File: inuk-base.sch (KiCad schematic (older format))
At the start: 4 parts

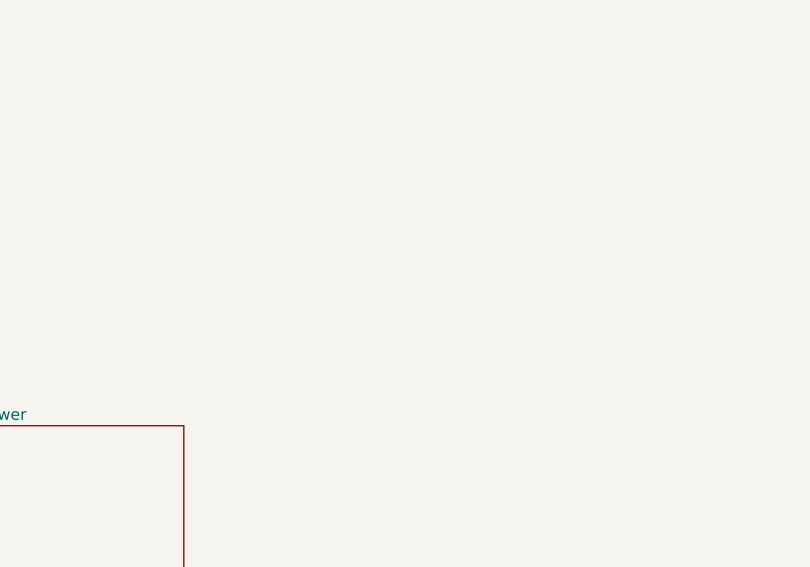
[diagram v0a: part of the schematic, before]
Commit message: created light control schematic
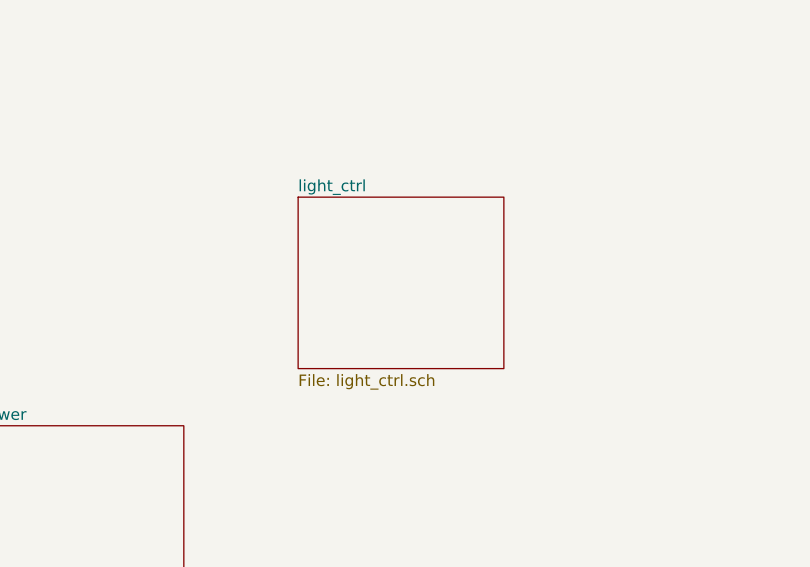
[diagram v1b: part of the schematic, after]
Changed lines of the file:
@@
 $Descr A4 11693 8268
 encoding utf-8
-Sheet 1 4
+Sheet 1 5
 Title ""
 Date ""
@@
 	1    0    0    -1
 $EndComp
+$Sheet
+S 6850 2350 900  750
+U 5E8399F7
+F0 "light_ctrl" 50
+F1 "light_ctrl.sch" 50
+$EndSheet
 $EndSCHEMATC

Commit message: layout
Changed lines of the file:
@@
 $EndDescr
 $Sheet
-S 2750 1750 1150 1400
+S 3750 2700 1150 1400
 U 5E59E010
 F0 "cpu" 50
 F1 "cpu.sch" 50
-F2 "uart_tx" O R 3900 1850 50
-F3 "uart_cts" I R 3900 2150 50
-F4 "uart_rts" O R 3900 2050 50
-F5 "uart_rx" I R 3900 1950 50
+F2 "uart_tx" O R 4900 2800 50
+F3 "uart_cts" I R 4900 3100 50
+F4 "uart_rts" O R 4900 3000 50
+F5 "uart_rx" I R 4900 2900 50
 $EndSheet
 $Sheet
-S 4400 1750 700  500
+S 5400 2700 700  500
 U 5E5A7255
 F0 "uart" 50
 F1 "uart.sch" 50
-F2 "uart_tx" I L 4400 1850 50
-F3 "uart_cts" O L 4400 2150 50
-F4 "uart_rts" I L 4400 2050 50
-F5 "uart_rx" O L 4400 1950 50
+F2 "uart_tx" I L 5400 2800 50
+F3 "uart_cts" O L 5400 3100 50
+F4 "uart_rts" I L 5400 3000 50
+F5 "uart_rx" O L 5400 2900 50
 $EndSheet
 $Sheet
-S 5450 3350 900  750
+S 5800 4300 900  750
 U 5E5BC499
 F0 "power" 50
@@
 $EndSheet
 Wire Wire Line
-	4400 1850 3900 1850
+	5400 2800 4900 2800
 Wire Wire Line
-	3900 1950 4400 1950
+	4900 2900 5400 2900
 Wire Wire Line
-	3900 2050 4400 2050
+	4900 3000 5400 3000
 Wire Wire Line
-	3900 2150 4400 2150
+	4900 3100 5400 3100
 $Comp
 L Mechanical:MountingHole H4
@@
 $EndComp
 $Sheet
-S 6850 2350 900  750
+S 7300 3300 900  750
 U 5E8399F7
 F0 "light_ctrl" 50

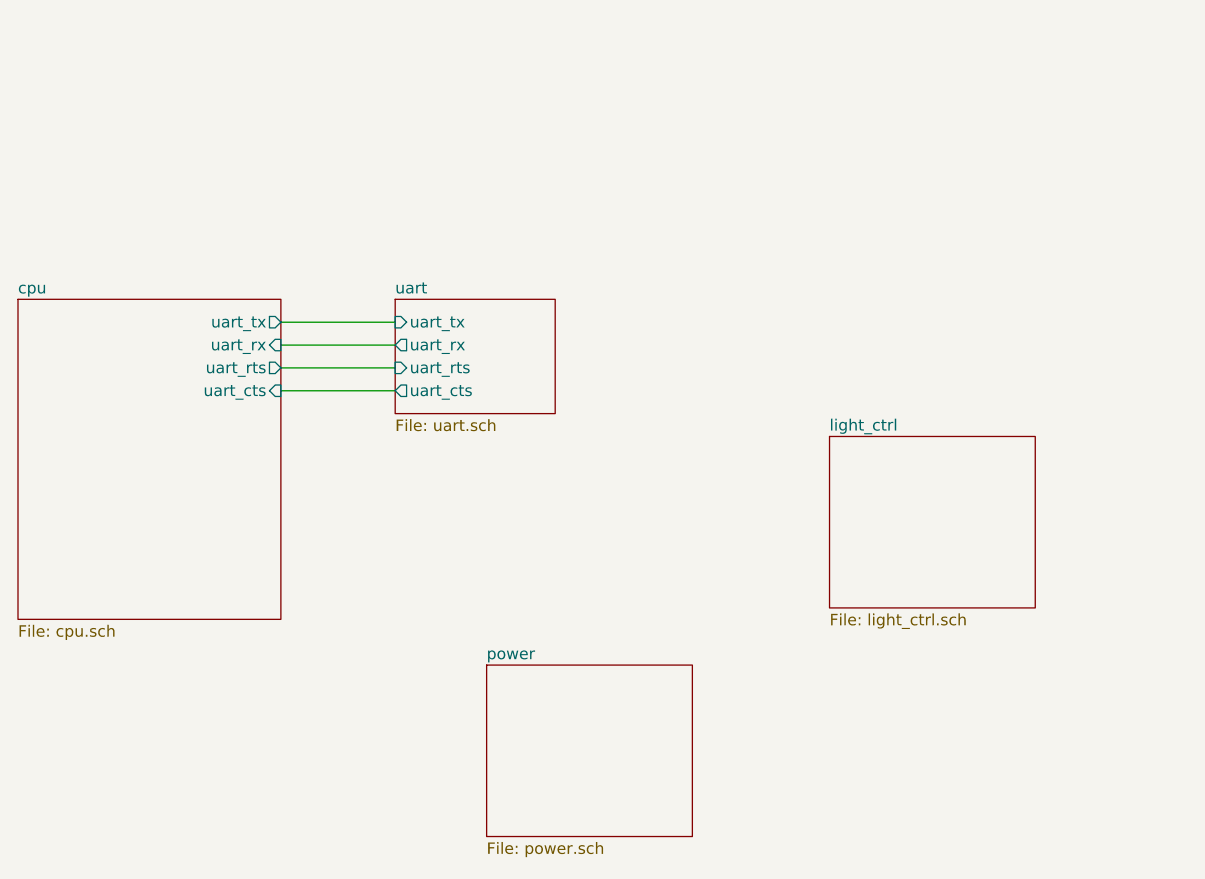
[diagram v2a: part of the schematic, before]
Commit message: added more circuit parts + new step files
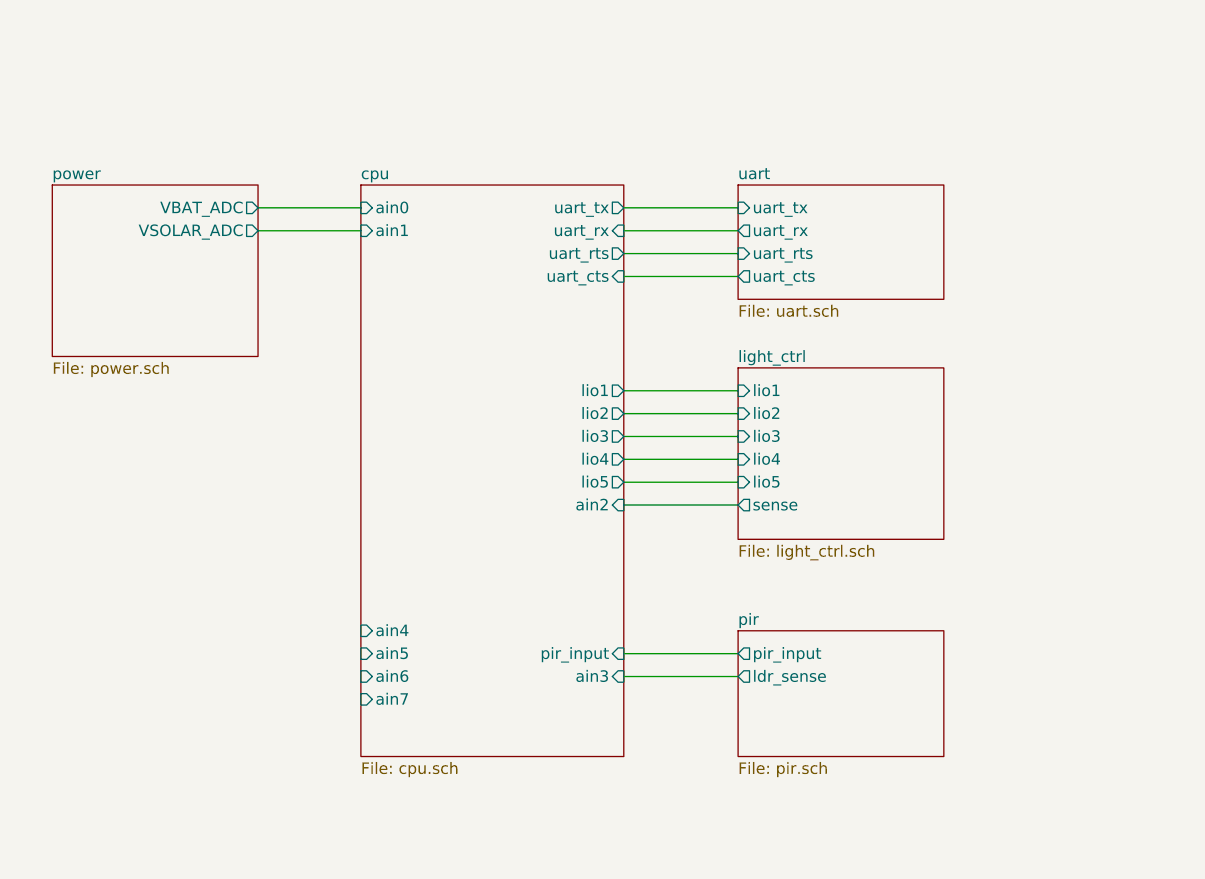
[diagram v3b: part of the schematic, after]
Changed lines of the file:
@@
 $Descr A4 11693 8268
 encoding utf-8
-Sheet 1 5
+Sheet 1 6
 Title ""
 Date ""
@@
 $EndDescr
 $Sheet
-S 3750 2700 1150 1400
-U 5E59E010
-F0 "cpu" 50
-F1 "cpu.sch" 50
-F2 "uart_tx" O R 4900 2800 50
-F3 "uart_cts" I R 4900 3100 50
-F4 "uart_rts" O R 4900 3000 50
-F5 "uart_rx" I R 4900 2900 50
-$EndSheet
-$Sheet
-S 5400 2700 700  500
+S 6900 2200 900  500
 U 5E5A7255
 F0 "uart" 50
 F1 "uart.sch" 50
-F2 "uart_tx" I L 5400 2800 50
-F3 "uart_cts" O L 5400 3100 50
-F4 "uart_rts" I L 5400 3000 50
-F5 "uart_rx" O L 5400 2900 50
+F2 "uart_tx" I L 6900 2300 50
+F3 "uart_cts" O L 6900 2600 50
+F4 "uart_rts" I L 6900 2500 50
+F5 "uart_rx" O L 6900 2400 50
 $EndSheet
 $Sheet
-S 5800 4300 900  750
+S 3900 2200 900  750
 U 5E5BC499
 F0 "power" 50
 F1 "power.sch" 50
+F2 "VBAT_ADC" O R 4800 2300 50
+F3 "VSOLAR_ADC" O R 4800 2400 50
 $EndSheet
 Wire Wire Line
-	5400 2800 4900 2800
+	6900 2300 6400 2300
 Wire Wire Line
-	4900 2900 5400 2900
+	6400 2400 6900 2400
 Wire Wire Line
-	4900 3000 5400 3000
+	6400 2500 6900 2500
 Wire Wire Line
-	4900 3100 5400 3100
+	6400 2600 6900 2600
 $Comp
 L Mechanical:MountingHole H4
@@
 $EndComp
 $Sheet
-S 7300 3300 900  750
+S 6900 3000 900  750
 U 5E8399F7
 F0 "light_ctrl" 50
 F1 "light_ctrl.sch" 50
+F2 "lio2" I L 6900 3200 50
+F3 "lio3" I L 6900 3300 50
+F4 "lio4" I L 6900 3400 50
+F5 "lio5" I L 6900 3500 50
+F6 "lio1" I L 6900 3100 50
+F7 "sense" O L 6900 3600 50
 $EndSheet
+Wire Wire Line
+	4800 2300 5250 2300
+Wire Wire Line
+	4800 2400 5250 2400
+Wire Wire Line
+	6900 3600 6400 3600
+$Sheet
+S 5250 2200 1150 2500
+U 5E59E010
+F0 "cpu" 50
+F1 "cpu.sch" 50
+F2 "uart_tx" O R 6400 2300 50
+F3 "uart_cts" I R 6400 2600 50
+F4 "uart_rts" O R 6400 2500 50
+F5 "uart_rx" I R 6400 2400 50
+F6 "ain0" I L 5250 2300 50
+F7 "ain1" I L 5250 2400 50
+F8 "ain2" I R 6400 3600 50
+F9 "ain3" I R 6400 4350 50
+F10 "ain4" I L 5250 4150 50
+F11 "ain5" I L 5250 4250 50
+F12 "ain6" I L 5250 4350 50
+F13 "ain7" I L 5250 4450 50
+F14 "lio1" O R 6400 3100 50
+F15 "lio2" O R 6400 3200 50
+F16 "lio3" O R 6400 3300 50
+F17 "lio4" O R 6400 3400 50
+F18 "lio5" O R 6400 3500 50
+F19 "pir_input" I R 6400 4250 50
+$EndSheet
+Wire Wire Line
+	6900 3100 6400 3100
+Wire Wire Line
+	6900 3200 6400 3200
+Wire Wire Line
+	6900 3300 6400 3300
+Wire Wire Line
+	6900 3400 6400 3400
+Wire Wire Line
+	6900 3500 6400 3500
+$Sheet
+S 6900 4150 900  550
+U 5E97BA81
+F0 "pir" 50
+F1 "pir.sch" 50
+F2 "pir_input" O L 6900 4250 50
+F3 "ldr_sense" O L 6900 4350 50
+$EndSheet
+Wire Wire Line
+	6900 4350 6400 4350
+Wire Wire Line
+	6400 4250 6900 4250
 $EndSCHEMATC

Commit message: started pcb routing
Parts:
- added U4: Logo_NM, Custom:Logo_NM, symbol Custom:Logo_NM
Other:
- moved on the sheet: H1, H2, H3, H4
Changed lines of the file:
@@
 $EndDescr
 $Sheet
-S 6900 2200 900  500
+S 6560 2670 900  500
 U 5E5A7255
 F0 "uart" 50
 F1 "uart.sch" 50
-F2 "uart_tx" I L 6900 2300 50
-F3 "uart_cts" O L 6900 2600 50
-F4 "uart_rts" I L 6900 2500 50
-F5 "uart_rx" O L 6900 2400 50
+F2 "uart_tx" I L 6560 2770 50
+F3 "uart_cts" O L 6560 3070 50
+F4 "uart_rts" I L 6560 2970 50
+F5 "uart_rx" O L 6560 2870 50
 $EndSheet
 $Sheet
-S 3900 2200 900  750
+S 3560 2670 900  750
 U 5E5BC499
 F0 "power" 50
 F1 "power.sch" 50
-F2 "VBAT_ADC" O R 4800 2300 50
-F3 "VSOLAR_ADC" O R 4800 2400 50
+F2 "VBAT_ADC" O R 4460 2770 50
+F3 "VSOLAR_ADC" O R 4460 2870 50
 $EndSheet
 Wire Wire Line
-	6900 2300 6400 2300
+	6560 2770 6060 2770
 Wire Wire Line
-	6400 2400 6900 2400
+	6060 2870 6560 2870
 Wire Wire Line
-	6400 2500 6900 2500
+	6060 2970 6560 2970
 Wire Wire Line
-	6400 2600 6900 2600
+	6060 3070 6560 3070
 $Comp
 L Mechanical:MountingHole H4
 U 1 1 5E7D5F82
-P 9550 1600
-F 0 "H4" H 9650 1646 50  0000 L CNN
-F 1 "MountingHole" H 9650 1555 50  0000 L CNN
-F 2 "MountingHole:MountingHole_3.2mm_M3_Pad_Via" H 9650 1509 50  0001 L CNN
-F 3 "~" H 9550 1600 50  0001 C CNN
-	1    9550 1600
+P 9600 1800
+F 0 "H4" H 9700 1846 50  0000 L CNN
+F 1 "MountingHole" H 9700 1755 50  0000 L CNN
+F 2 "MountingHole:MountingHole_3.2mm_M3_Pad_Via" H 9700 1709 50  0001 L CNN
+F 3 "~" H 9600 1800 50  0001 C CNN
+	1    9600 1800
 	1    0    0    -1
 $EndComp
@@
 L Mechanical:MountingHole H3
 U 1 1 5E7D615B
-P 9550 1400
-F 0 "H3" H 9650 1446 50  0000 L CNN
-F 1 "MountingHole" H 9650 1355 50  0000 L CNN
-F 2 "MountingHole:MountingHole_3.2mm_M3_Pad_Via" H 9650 1309 50  0001 L CNN
-F 3 "~" H 9550 1400 50  0001 C CNN
-	1    9550 1400
+P 9600 1600
+F 0 "H3" H 9700 1646 50  0000 L CNN
+F 1 "MountingHole" H 9700 1555 50  0000 L CNN
+F 2 "MountingHole:MountingHole_3.2mm_M3_Pad_Via" H 9700 1509 50  0001 L CNN
+F 3 "~" H 9600 1600 50  0001 C CNN
+	1    9600 1600
 	1    0    0    -1
 $EndComp
@@
 L Mechanical:MountingHole H2
 U 1 1 5E7D677D
-P 9550 1200
-F 0 "H2" H 9650 1246 50  0000 L CNN
-F 1 "MountingHole" H 9650 1155 50  0000 L CNN
-F 2 "MountingHole:MountingHole_3.2mm_M3_Pad_Via" H 9650 1109 50  0001 L CNN
-F 3 "~" H 9550 1200 50  0001 C CNN
-	1    9550 1200
+P 9600 1400
+F 0 "H2" H 9700 1446 50  0000 L CNN
+F 1 "MountingHole" H 9700 1355 50  0000 L CNN
+F 2 "MountingHole:MountingHole_3.2mm_M3_Pad_Via" H 9700 1309 50  0001 L CNN
+F 3 "~" H 9600 1400 50  0001 C CNN
+	1    9600 1400
 	1    0    0    -1
 $EndComp
@@
 L Mechanical:MountingHole H1
 U 1 1 5E7D6AF7
-P 9550 1000
-F 0 "H1" H 9650 1046 50  0000 L CNN
-F 1 "MountingHole" H 9650 955 50  0000 L CNN
-F 2 "MountingHole:MountingHole_3.2mm_M3_Pad_Via" H 9650 909 50  0001 L CNN
-F 3 "~" H 9550 1000 50  0001 C CNN
-	1    9550 1000
+P 9600 1200
+F 0 "H1" H 9700 1246 50  0000 L CNN
+F 1 "MountingHole" H 9700 1155 50  0000 L CNN
+F 2 "MountingHole:MountingHole_3.2mm_M3_Pad_Via" H 9700 1109 50  0001 L CNN
+F 3 "~" H 9600 1200 50  0001 C CNN
+	1    9600 1200
 	1    0    0    -1
 $EndComp
 $Sheet
-S 6900 3000 900  750
+S 6560 3470 900  750
 U 5E8399F7
 F0 "light_ctrl" 50
 F1 "light_ctrl.sch" 50
-F2 "lio2" I L 6900 3200 50
-F3 "lio3" I L 6900 3300 50
-F4 "lio4" I L 6900 3400 50
-F5 "lio5" I L 6900 3500 50
-F6 "lio1" I L 6900 3100 50
-F7 "sense" O L 6900 3600 50
+F2 "lio2" I L 6560 3670 50
+F3 "lio3" I L 6560 3770 50
+F4 "lio4" I L 6560 3870 50
+F5 "lio5" I L 6560 3970 50
+F6 "lio1" I L 6560 3570 50
+F7 "sense" O L 6560 4070 50
 $EndSheet
 Wire Wire Line
-	4800 2300 5250 2300
+	4460 2770 4910 2770
 Wire Wire Line
-	4800 2400 5250 2400
+	4460 2870 4910 2870
 Wire Wire Line
-	6900 3600 6400 3600
+	6560 4070 6060 4070
 $Sheet
-S 5250 2200 1150 2500
+S 4910 2670 1150 2500
 U 5E59E010
 F0 "cpu" 50
 F1 "cpu.sch" 50
-F2 "uart_tx" O R 6400 2300 50
-F3 "uart_cts" I R 6400 2600 50
-F4 "uart_rts" O R 6400 2500 50
-F5 "uart_rx" I R 6400 2400 50
-F6 "ain0" I L 5250 2300 50
-F7 "ain1" I L 5250 2400 50
-F8 "ain2" I R 6400 3600 50
-F9 "ain3" I R 6400 4350 50
-F10 "ain4" I L 5250 4150 50
-F11 "ain5" I L 5250 4250 50
-F12 "ain6" I L 5250 4350 50
-F13 "ain7" I L 5250 4450 50
-F14 "lio1" O R 6400 3100 50
-F15 "lio2" O R 6400 3200 50
-F16 "lio3" O R 6400 3300 50
-F17 "lio4" O R 6400 3400 50
-F18 "lio5" O R 6400 3500 50
-F19 "pir_input" I R 6400 4250 50
+F2 "uart_tx" O R 6060 2770 50
+F3 "uart_cts" I R 6060 3070 50
+F4 "uart_rts" O R 6060 2970 50
+F5 "uart_rx" I R 6060 2870 50
+F6 "ain0" I L 4910 2770 50
+F7 "ain1" I L 4910 2870 50
+F8 "ain2" I R 6060 4070 50
+F9 "ain3" I R 6060 4820 50
+F10 "ain4" I L 4910 4620 50
+F11 "ain5" I L 4910 4720 50
+F12 "ain6" I L 4910 4820 50
+F13 "ain7" I L 4910 4920 50
+F14 "lio1" O R 6060 3570 50
+F15 "lio2" O R 6060 3670 50
+F16 "lio3" O R 6060 3770 50
+F17 "lio4" O R 6060 3870 50
+F18 "lio5" O R 6060 3970 50
+F19 "pir_input" I R 6060 4720 50
 $EndSheet
 Wire Wire Line
-	6900 3100 6400 3100
+	6560 3570 6060 3570
 Wire Wire Line
-	6900 3200 6400 3200
+	6560 3670 6060 3670
 Wire Wire Line
-	6900 3300 6400 3300
+	6560 3770 6060 3770
 Wire Wire Line
-	6900 3400 6400 3400
+	6560 3870 6060 3870
 Wire Wire Line
-	6900 3500 6400 3500
+	6560 3970 6060 3970
 $Sheet
-S 6900 4150 900  550
+S 6560 4620 900  550
 U 5E97BA81
 F0 "pir" 50
 F1 "pir.sch" 50
-F2 "pir_input" O L 6900 4250 50
-F3 "ldr_sense" O L 6900 4350 50
+F2 "pir_input" O L 6560 4720 50
+F3 "ldr_sense" O L 6560 4820 50
 $EndSheet
 Wire Wire Line
-	6900 4350 6400 4350
+	6560 4820 6060 4820
 Wire Wire Line
-	6400 4250 6900 4250
+	6060 4720 6560 4720
+$Comp
+L Custom:Logo_NM U4
+U 1 1 5EB7B6B6
+P 9600 2090
+F 0 "U4" H 9500 2140 50  0001 C CNN
+F 1 "Logo_NM" H 9695 2124 50  0000 L CNN
+F 2 "Custom:Logo_NM" H 9644 2020 50  0001 C CNN
+F 3 "" H 9540 2076 50  0001 C CNN
+	1    9600 2090
+	1    0    0    -1
+$EndComp
 $EndSCHEMATC
